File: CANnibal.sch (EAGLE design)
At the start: 22 parts, among them J1 POGOPIN-CONN-4, J3 455-1750-1-ND, J6 455-1750-1-ND, U1 STM32F042C6T6, U2 MF-REG-SOT235-3.3V-300mA

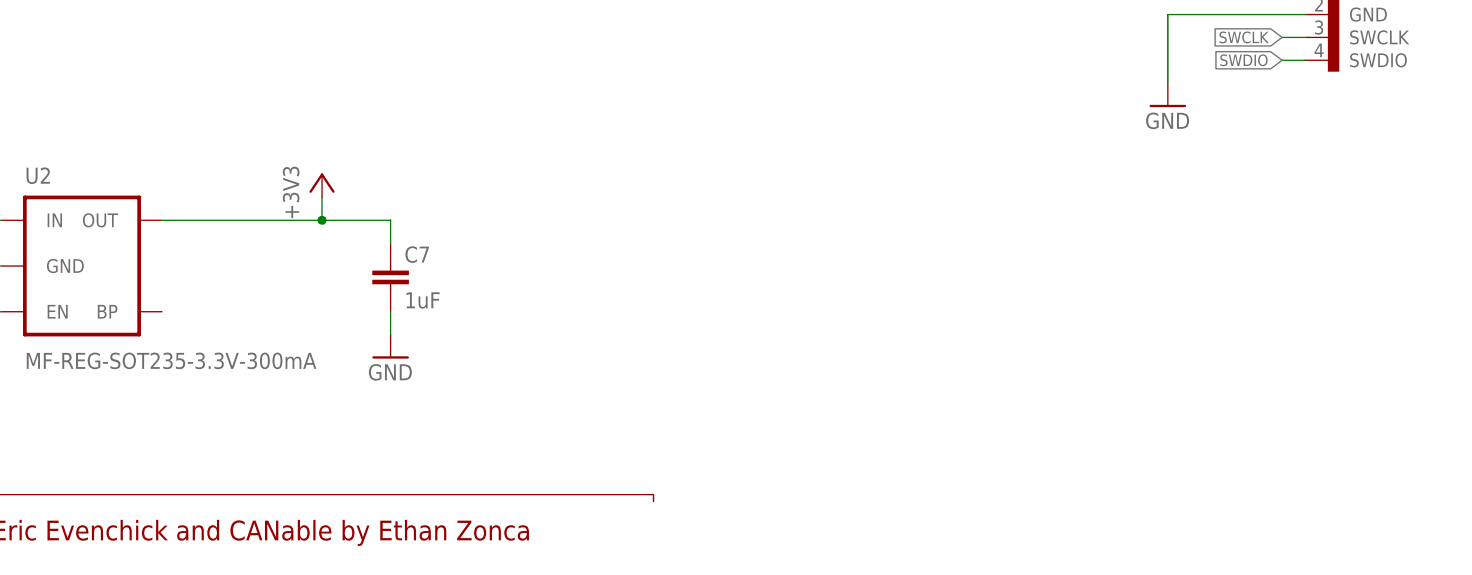
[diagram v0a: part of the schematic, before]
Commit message: Final version
Updates USB footprint, fiducials, images, etc
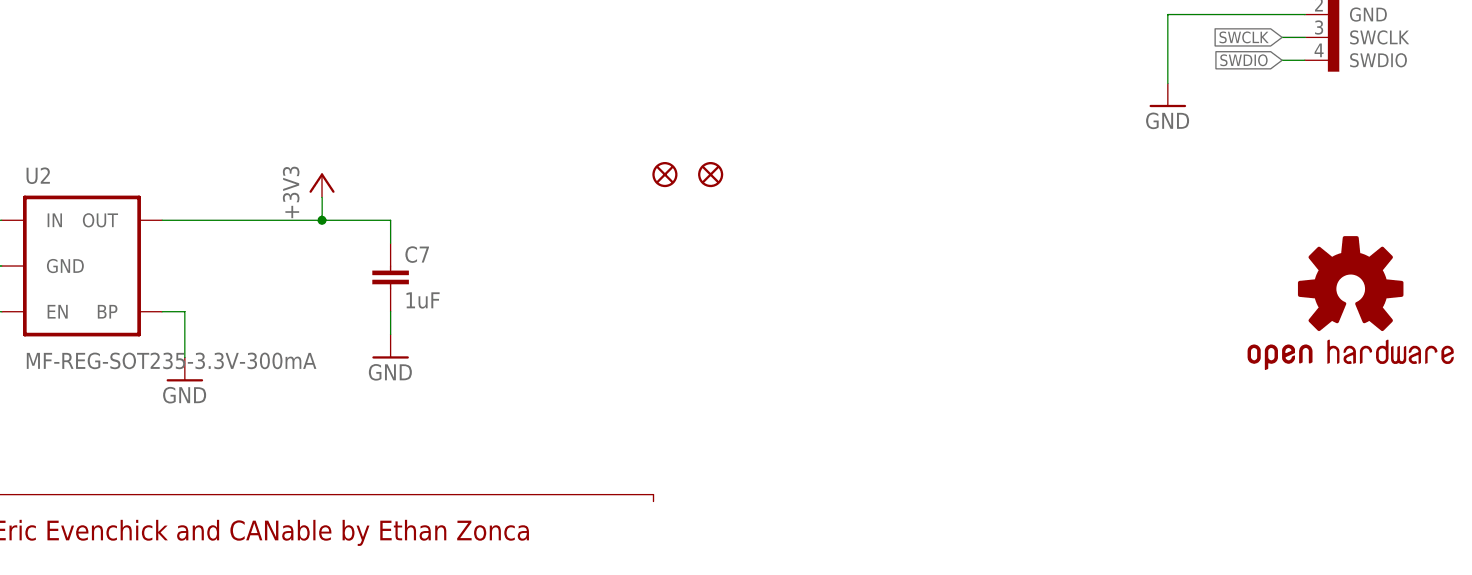
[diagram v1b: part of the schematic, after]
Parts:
- added FD1, FD2: FIDUCIAL1X2, SparkFun-Aesthetics:FIDUCIAL1X2
- added LOGO1: OSHW-LOGOS, SparkFun-Aesthetics:OSHW-LOGOS
- U$4: device micro usb B - 4LEGS:MICRO-USB-B -> pmc_lib:MICRO-USB-B
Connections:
- net GND: now also U2.BP
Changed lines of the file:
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@@
 <part name="F1" library="dp_devices" deviceset="FUSE_PTC" device="-0805" value="0ZCK0035FF2G"/>
 <part name="U$1" library="microbuilder" deviceset="GND" device=""/>
-<part name="U$4" library="micro usb B - 4LEGS" deviceset="MICRO-USB-B" device=""/>
+<part name="U$4" library="pmc_lib" deviceset="MICRO-USB-B" device="" package3d_urn="urn:adsk.eagle:package:7651683/2"/>
 <part name="P+1" library="supply1" library_urn="urn:adsk.eagle:library:371" deviceset="+5V" device=""/>
 <part name="P+3" library="supply1" library_urn="urn:adsk.eagle:library:371" deviceset="+5V" device=""/>
@@
 <part name="+3V5" library="supply1" library_urn="urn:adsk.eagle:library:371" deviceset="+3V3" device=""/>
 <part name="+3V6" library="supply1" library_urn="urn:adsk.eagle:library:371" deviceset="+3V3" device=""/>
+<part name="GND12" library="SparkFun-Aesthetics" deviceset="GND" device=""/>
+<part name="FD1" library="SparkFun-Aesthetics" deviceset="FIDUCIAL" device="1X2"/>
+<part name="FD2" library="SparkFun-Aesthetics" deviceset="FIDUCIAL" device="1X2"/>
+<part name="LOGO1" library="SparkFun-Aesthetics" deviceset="OSHW-LOGO" device="S"/>
 </parts>
 <sheets>
@@
 <attribute name="VALUE" x="246.38" y="96.52" size="1.778" layer="96" rot="R90"/>
 </instance>
+<instance part="GND12" gate="1" x="132.08" y="25.4" smashed="yes">
+<attribute name="VALUE" x="129.54" y="22.86" size="1.778" layer="96"/>
+</instance>
+<instance part="FD1" gate="G$1" x="185.42" y="48.26" smashed="yes"/>
+<instance part="FD2" gate="G$1" x="190.5" y="48.26" smashed="yes"/>
+<instance part="LOGO1" gate="G$1" x="261.62" y="35.56" smashed="yes"/>
 </instances>
 <busses>
@@
 <pinref part="DA1" gate="G$1" pin="RS"/>
 <wire x1="236.22" y1="96.52" x2="241.3" y2="96.52" width="0.1524" layer="91"/>
+</segment>
+<segment>
+<pinref part="U2" gate="G$1" pin="BP"/>
+<pinref part="GND12" gate="1" pin="GND"/>
+<wire x1="129.54" y1="33.02" x2="132.08" y2="33.02" width="0.1524" layer="91"/>
+<wire x1="132.08" y1="33.02" x2="132.08" y2="27.94" width="0.1524" layer="91"/>
 </segment>
 </net>
@@
 will not be understood (or retained) with this version.
 </note>
+<note version="8.3" severity="warning">
+Since Version 8.3, EAGLE supports the association of 3D packages
+with devices in libraries, schematics, and board files. Those 3D
+packages will not be understood (or retained) with this version.
+</note>
 </compatibility>
